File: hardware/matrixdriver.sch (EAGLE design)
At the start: 50 parts, among them IC1 75176AD, IC2 4017D, IC3 ULN2803, IC4 7805DT, Q1 20MHZ, Q2 MMBT4403LT1SMD, Q3 MMBT4403LT1SMD, Q4 MMBT4403LT1SMD, Q5 MMBT4403LT1SMD, Q6 MMBT4403LT1SMD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

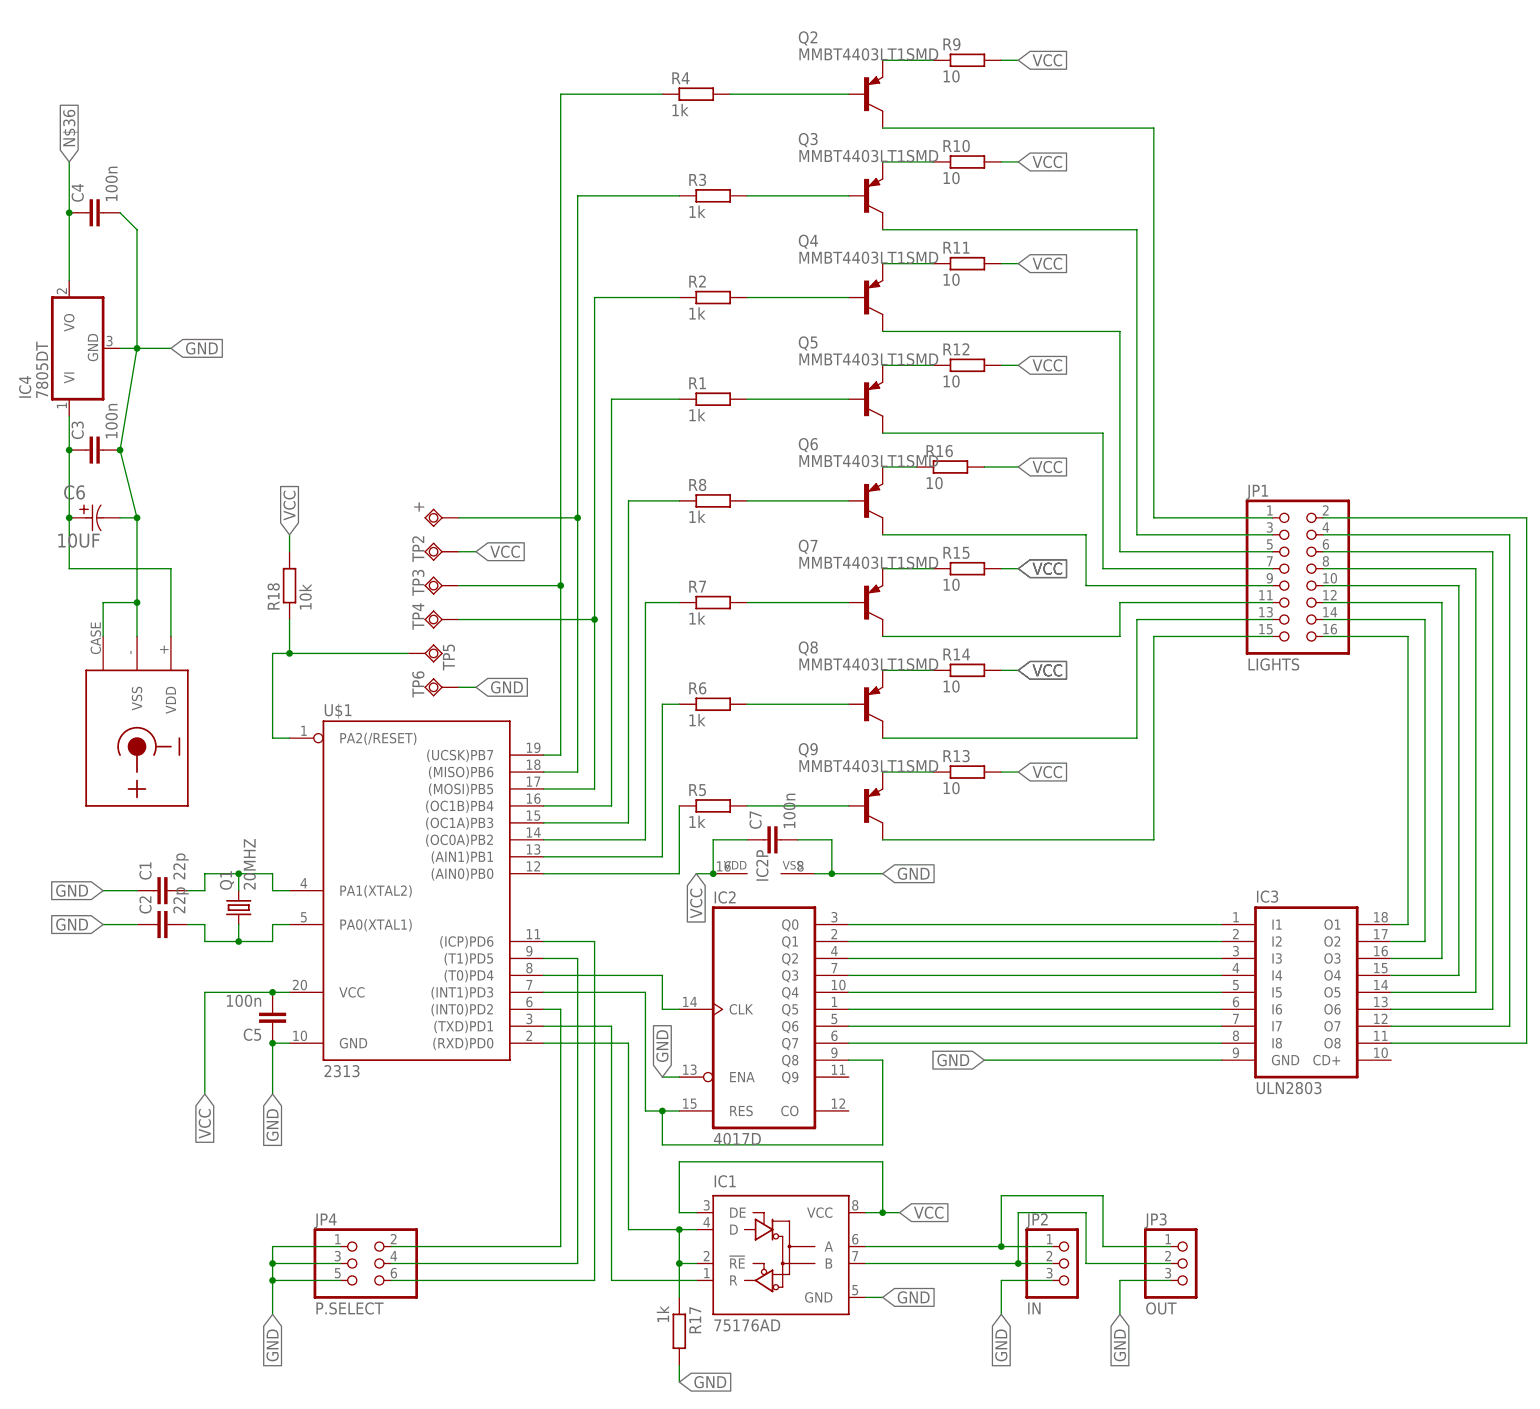
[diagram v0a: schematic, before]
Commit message: transistor block changed
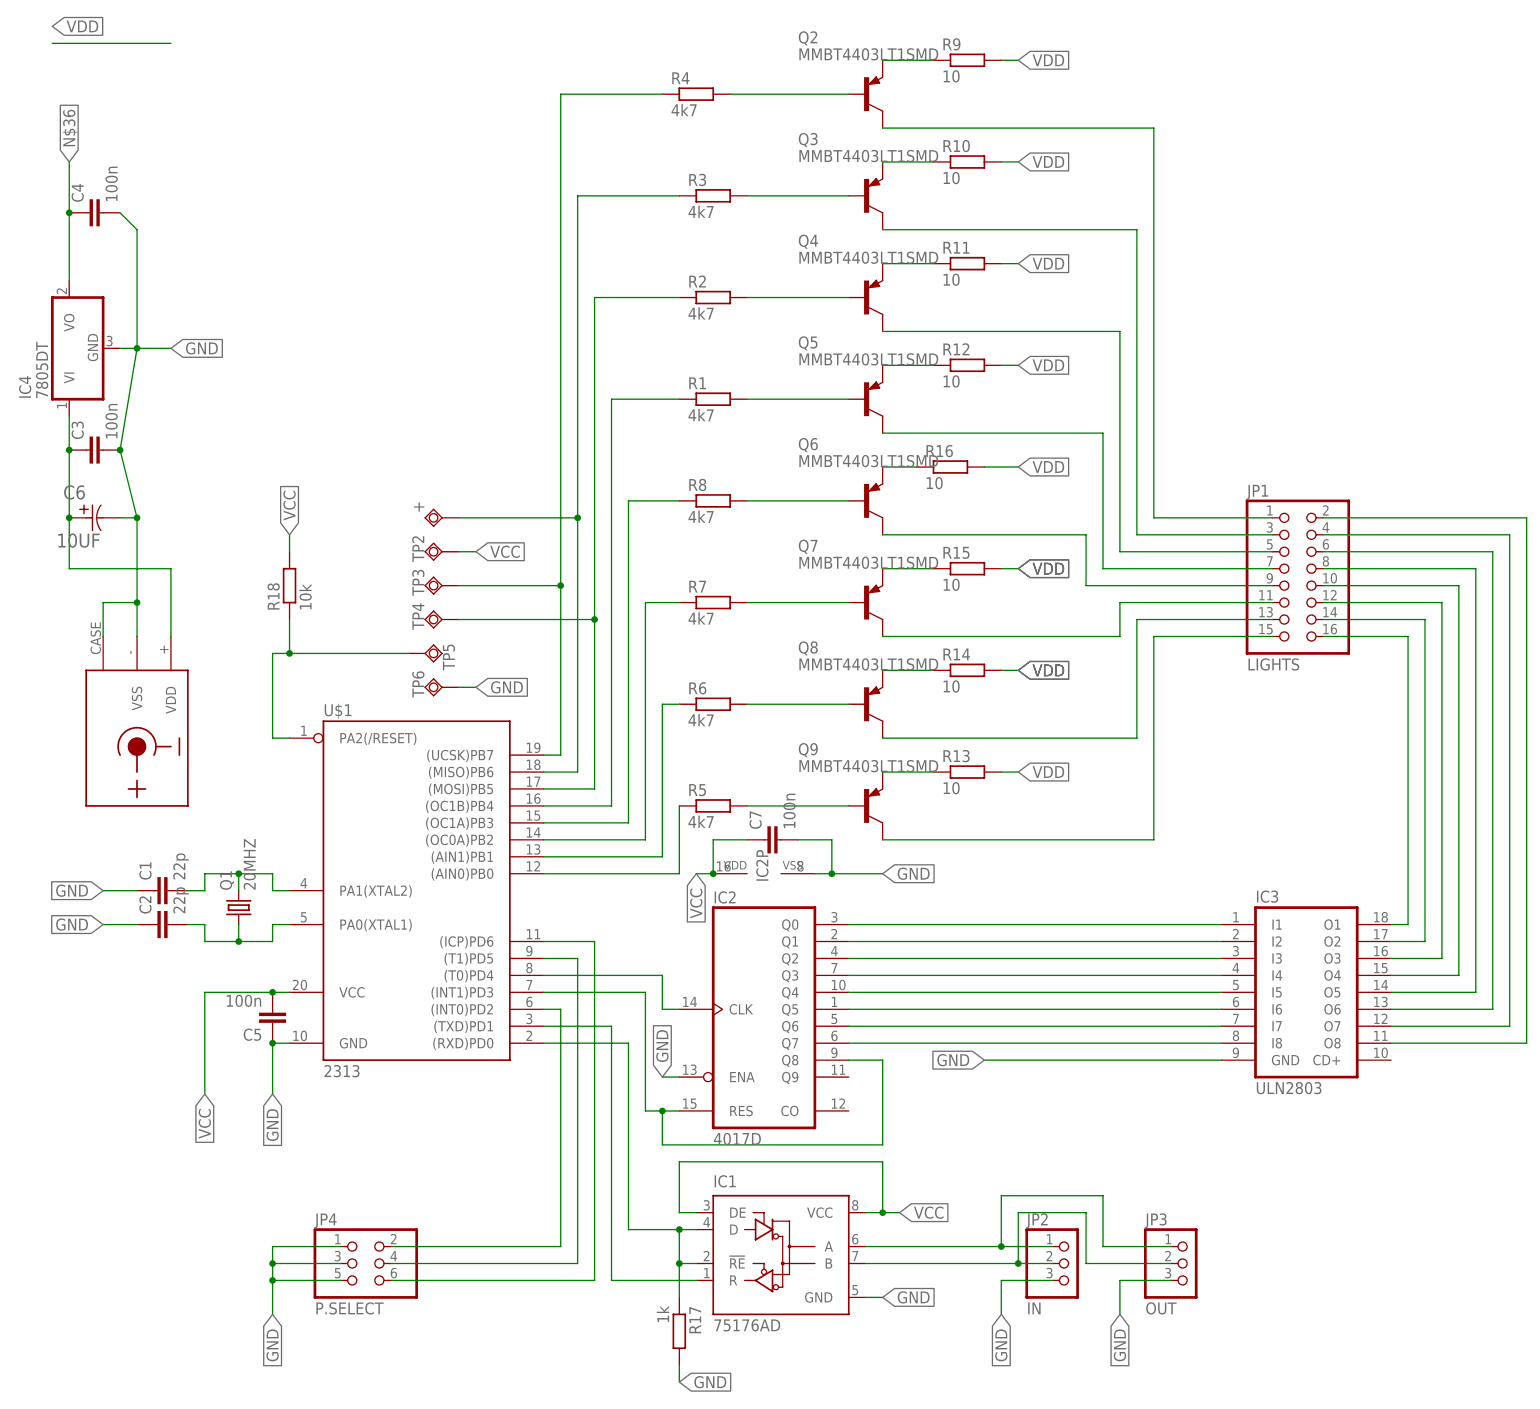
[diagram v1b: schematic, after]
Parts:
- R1, R2, R3, R4, R5, R6, R7, R8: value 1k -> 4k7
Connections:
- new net VDD: R10.2, R11.2, R12.2, R13.2, R14.2, R15.2, R16.2, R9.2
- net VCC: no longer R10.2, R11.2, R12.2, R13.2, R14.2, R15.2, R16.2, R9.2
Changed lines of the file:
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@@
 <part name="Q1" library="crystal" deviceset="CRYSTAL" device="HC49UP" value="20MHZ"/>
 <part name="U$2" library="con-dc-jack" deviceset="CUI_PJ-102A" device=""/>
-<part name="R2" library="resistor" deviceset="R-EU_" device="R1206" value="1k"/>
-<part name="R1" library="resistor" deviceset="R-EU_" device="R1206" value="1k"/>
-<part name="R3" library="resistor" deviceset="R-EU_" device="R1206" value="1k"/>
-<part name="R4" library="resistor" deviceset="R-EU_" device="R1206" value="1k"/>
-<part name="R5" library="resistor" deviceset="R-EU_" device="R1206" value="1k"/>
-<part name="R6" library="resistor" deviceset="R-EU_" device="R1206" value="1k"/>
-<part name="R7" library="resistor" deviceset="R-EU_" device="R1206" value="1k"/>
-<part name="R8" library="resistor" deviceset="R-EU_" device="R1206" value="1k"/>
+<part name="R2" library="resistor" deviceset="R-EU_" device="R1206" value="4k7"/>
+<part name="R1" library="resistor" deviceset="R-EU_" device="R1206" value="4k7"/>
+<part name="R3" library="resistor" deviceset="R-EU_" device="R1206" value="4k7"/>
+<part name="R4" library="resistor" deviceset="R-EU_" device="R1206" value="4k7"/>
+<part name="R5" library="resistor" deviceset="R-EU_" device="R1206" value="4k7"/>
+<part name="R6" library="resistor" deviceset="R-EU_" device="R1206" value="4k7"/>
+<part name="R7" library="resistor" deviceset="R-EU_" device="R1206" value="4k7"/>
+<part name="R8" library="resistor" deviceset="R-EU_" device="R1206" value="4k7"/>
 <part name="R9" library="resistor" deviceset="R-EU_" device="R1206" value="10"/>
 <part name="R10" library="resistor" deviceset="R-EU_" device="R1206" value="10"/>
@@
 <net name="VCC" class="0">
 <segment>
-<wire x1="144.78" y1="195.58" x2="147.32" y2="195.58" width="0.1524" layer="91"/>
-<pinref part="R9" gate="G$1" pin="2"/>
-<label x="147.32" y="195.58" size="1.778" layer="95" xref="yes"/>
-</segment>
-<segment>
-<pinref part="R12" gate="G$1" pin="2"/>
-<wire x1="144.78" y1="149.86" x2="147.32" y2="149.86" width="0.1524" layer="91"/>
-<label x="147.32" y="149.86" size="1.778" layer="95" xref="yes"/>
-</segment>
-<segment>
-<wire x1="144.78" y1="165.1" x2="147.32" y2="165.1" width="0.1524" layer="91"/>
-<label x="147.32" y="165.1" size="1.778" layer="95" xref="yes"/>
-<pinref part="R11" gate="G$1" pin="2"/>
-</segment>
-<segment>
-<pinref part="R10" gate="G$1" pin="2"/>
-<wire x1="144.78" y1="180.34" x2="147.32" y2="180.34" width="0.1524" layer="91"/>
-<label x="147.32" y="180.34" size="1.778" layer="95" xref="yes"/>
-</segment>
-<segment>
-<wire x1="142.24" y1="134.62" x2="147.32" y2="134.62" width="0.1524" layer="91"/>
-<label x="147.32" y="134.62" size="1.778" layer="95" xref="yes"/>
-<pinref part="R16" gate="G$1" pin="2"/>
-</segment>
-<segment>
-<wire x1="144.78" y1="119.38" x2="147.32" y2="119.38" width="0.1524" layer="91"/>
-<label x="147.32" y="119.38" size="1.778" layer="95" xref="yes"/>
-<label x="147.32" y="119.38" size="1.778" layer="95" xref="yes"/>
-<pinref part="R15" gate="G$1" pin="2"/>
-</segment>
-<segment>
-<wire x1="144.78" y1="104.14" x2="147.32" y2="104.14" width="0.1524" layer="91"/>
-<label x="147.32" y="104.14" size="1.778" layer="95" xref="yes"/>
-<label x="147.32" y="104.14" size="1.778" layer="95" xref="yes"/>
-<pinref part="R14" gate="G$1" pin="2"/>
-</segment>
-<segment>
 <pinref part="IC1" gate="G$1" pin="DE"/>
 <wire x1="99.06" y1="22.86" x2="96.52" y2="22.86" width="0.1524" layer="91"/>
@@
 <label x="38.1" y="124.46" size="1.778" layer="95" rot="R90" xref="yes"/>
 </segment>
-<segment>
-<pinref part="R13" gate="G$1" pin="2"/>
-<wire x1="144.78" y1="88.9" x2="147.32" y2="88.9" width="0.1524" layer="91"/>
-<label x="147.32" y="88.9" size="1.778" layer="95" xref="yes"/>
-</segment>
 </net>
 <net name="N$34" class="0">
@@
 </segment>
 </net>
+<net name="VDD" class="0">
+<segment>
+<wire x1="2.54" y1="198.12" x2="20.32" y2="198.12" width="0.1524" layer="91"/>
+<label x="2.54" y="200.66" size="1.778" layer="95" xref="yes"/>
+</segment>
+<segment>
+<wire x1="144.78" y1="195.58" x2="147.32" y2="195.58" width="0.1524" layer="91"/>
+<pinref part="R9" gate="G$1" pin="2"/>
+<label x="147.32" y="195.58" size="1.778" layer="95" xref="yes"/>
+</segment>
+<segment>
+<pinref part="R10" gate="G$1" pin="2"/>
+<wire x1="144.78" y1="180.34" x2="147.32" y2="180.34" width="0.1524" layer="91"/>
+<label x="147.32" y="180.34" size="1.778" layer="95" xref="yes"/>
+</segment>
+<segment>
+<wire x1="144.78" y1="165.1" x2="147.32" y2="165.1" width="0.1524" layer="91"/>
+<label x="147.32" y="165.1" size="1.778" layer="95" xref="yes"/>
+<pinref part="R11" gate="G$1" pin="2"/>
+</segment>
+<segment>
+<pinref part="R12" gate="G$1" pin="2"/>
+<wire x1="144.78" y1="149.86" x2="147.32" y2="149.86" width="0.1524" layer="91"/>
+<label x="147.32" y="149.86" size="1.778" layer="95" xref="yes"/>
+</segment>
+<segment>
+<wire x1="142.24" y1="134.62" x2="147.32" y2="134.62" width="0.1524" layer="91"/>
+<label x="147.32" y="134.62" size="1.778" layer="95" xref="yes"/>
+<pinref part="R16" gate="G$1" pin="2"/>
+</segment>
+<segment>
+<wire x1="144.78" y1="119.38" x2="147.32" y2="119.38" width="0.1524" layer="91"/>
+<label x="147.32" y="119.38" size="1.778" layer="95" xref="yes"/>
+<label x="147.32" y="119.38" size="1.778" layer="95" xref="yes"/>
+<pinref part="R15" gate="G$1" pin="2"/>
+</segment>
+<segment>
+<wire x1="144.78" y1="104.14" x2="147.32" y2="104.14" width="0.1524" layer="91"/>
+<label x="147.32" y="104.14" size="1.778" layer="95" xref="yes"/>
+<label x="147.32" y="104.14" size="1.778" layer="95" xref="yes"/>
+<pinref part="R14" gate="G$1" pin="2"/>
+</segment>
+<segment>
+<pinref part="R13" gate="G$1" pin="2"/>
+<wire x1="144.78" y1="88.9" x2="147.32" y2="88.9" width="0.1524" layer="91"/>
+<label x="147.32" y="88.9" size="1.778" layer="95" xref="yes"/>
+</segment>
+</net>

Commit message: Beschriftungen angepasst
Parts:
- Q3, Q4, Q5, Q6, Q7, Q8, Q9: value MMBT4403LT1SMD -> BC856
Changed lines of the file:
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@@
 <part name="JP1" library="pinhead-fixdrills" deviceset="PINHD-2X8" device="_2.54" value="LIGHTS"/>
 <part name="Q2" library="transistor-pnp" deviceset="MMBT4403*" device="SMD" technology="LT1"/>
-<part name="Q3" library="transistor-pnp" deviceset="MMBT4403*" device="SMD" technology="LT1"/>
-<part name="Q4" library="transistor-pnp" deviceset="MMBT4403*" device="SMD" technology="LT1"/>
-<part name="Q5" library="transistor-pnp" deviceset="MMBT4403*" device="SMD" technology="LT1"/>
-<part name="Q6" library="transistor-pnp" deviceset="MMBT4403*" device="SMD" technology="LT1"/>
-<part name="Q7" library="transistor-pnp" deviceset="MMBT4403*" device="SMD" technology="LT1"/>
-<part name="Q8" library="transistor-pnp" deviceset="MMBT4403*" device="SMD" technology="LT1"/>
-<part name="Q9" library="transistor-pnp" deviceset="MMBT4403*" device="SMD" technology="LT1"/>
+<part name="Q3" library="transistor-pnp" deviceset="MMBT4403*" device="SMD" technology="LT1" value="BC856"/>
+<part name="Q4" library="transistor-pnp" deviceset="MMBT4403*" device="SMD" technology="LT1" value="BC856"/>
+<part name="Q5" library="transistor-pnp" deviceset="MMBT4403*" device="SMD" technology="LT1" value="BC856"/>
+<part name="Q6" library="transistor-pnp" deviceset="MMBT4403*" device="SMD" technology="LT1" value="BC856"/>
+<part name="Q7" library="transistor-pnp" deviceset="MMBT4403*" device="SMD" technology="LT1" value="BC856"/>
+<part name="Q8" library="transistor-pnp" deviceset="MMBT4403*" device="SMD" technology="LT1" value="BC856"/>
+<part name="Q9" library="transistor-pnp" deviceset="MMBT4403*" device="SMD" technology="LT1" value="BC856"/>
 <part name="JP2" library="pinhead" deviceset="PINHD-1X3" device="" value="IN"/>
 <part name="JP3" library="pinhead" deviceset="PINHD-1X3" device="" value="OUT"/>
@@
 <net name="VDD" class="0">
 <segment>
-<wire x1="2.54" y1="198.12" x2="20.32" y2="198.12" width="0.1524" layer="91"/>
-<label x="2.54" y="200.66" size="1.778" layer="95" xref="yes"/>
-</segment>
-<segment>
+<wire x1="5.08" y1="198.12" x2="20.32" y2="198.12" width="0.1524" layer="91"/>
+<label x="5.08" y="197.358" size="1.778" layer="95" rot="R270" xref="yes"/>
+</segment>
+<segment>
